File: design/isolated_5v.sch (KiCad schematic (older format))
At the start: 10 parts, among them T1 TRANS-2CT, U2 SN6501DBV, U4 TPS76350

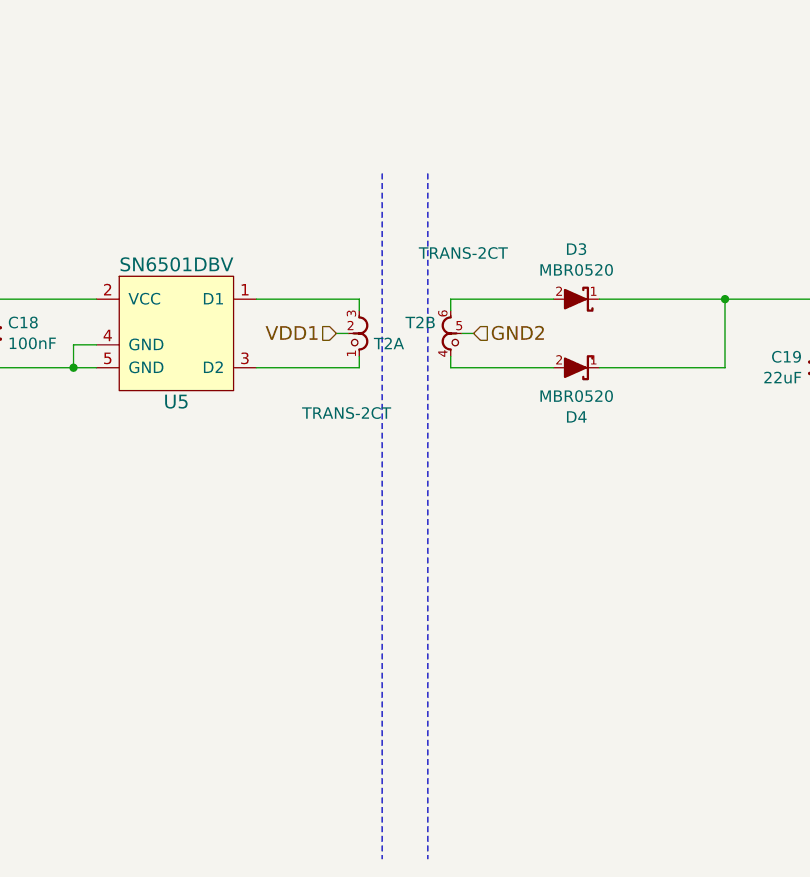
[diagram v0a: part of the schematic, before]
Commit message: Added buffer to restore signal before opamp analog filter
Signed-off-by: Marcos Chaparro <mchaparro@paltatech.com>
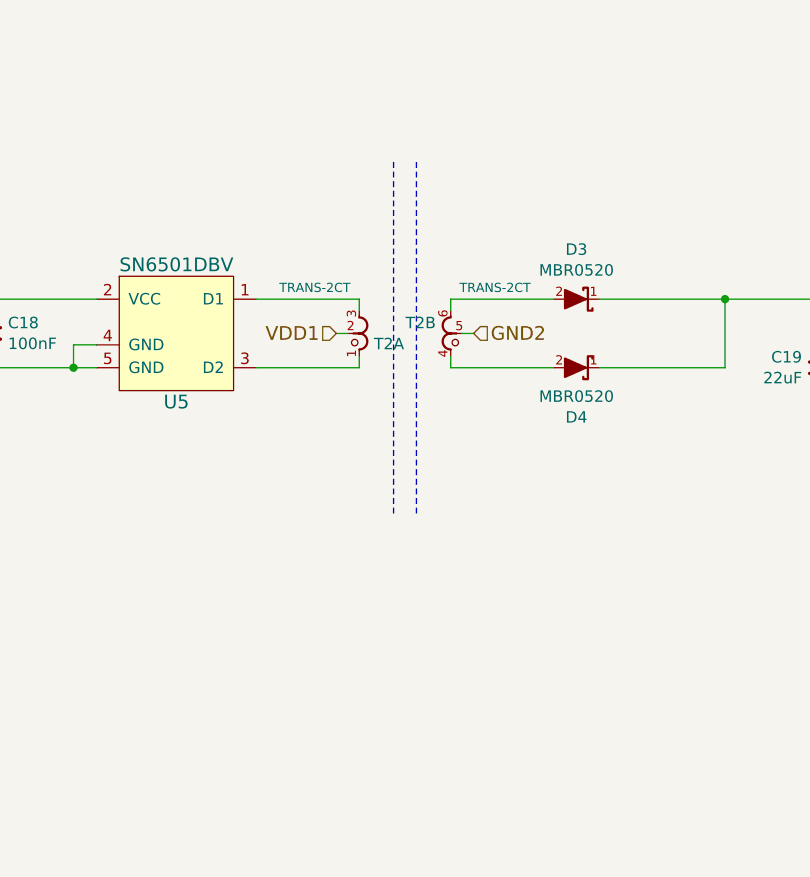
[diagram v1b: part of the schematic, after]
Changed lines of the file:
@@
 AR Path="/598FD5E6/589DB385" Ref="T2"  Part="1"
 F 0 "T2" H 4736 3096 50  0000 R CNN
-F 1 "TRANS-2CT" H 5050 3400 50  0000 R CNN
+F 1 "TRANS-2CT" H 5150 2850 40  0000 R CNN
 F 2 "manuf:WURTH-760390014" H 4650 2800 60  0001 C CNN
 F 3 "http://katalog.we-online.de/ctm/datasheet/760390014.pdf" H -1000 850 60  0001 C CNN
@@
 AR Path="/598FD5E6/589DB38D" Ref="T2"  Part="2"
 F 0 "T2" H 5135 3004 50  0000 R CNN
-F 1 "TRANS-2CT" H 5450 2700 50  0000 R CNN
+F 1 "TRANS-2CT" H 5550 2850 40  0000 R CNN
 F 2 "manuf:WURTH-760390014" H 5100 3400 60  0001 C CNN
 F 3 "http://katalog.we-online.de/ctm/datasheet/760390014.pdf" H -450 850 60  0001 C CNN
@@
 Text HLabel 8600 3500 2    60   Input ~ 0
 GND2
-Wire Notes Line
-	5100 2350 5100 5350
-Wire Notes Line
-	4900 2350 4900 5350
 Wire Wire Line
 	3650 3200 2600 3200
@@
 Text Notes 1350 1600 0    160  ~ 32
 ISOLATED POWER SUPPLY
+Wire Notes Line
+	4950 2300 4950 3850
+Wire Notes Line
+	5050 2300 5050 3850
 $EndSCHEMATC
